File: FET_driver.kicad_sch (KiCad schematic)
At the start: 48 parts, among them Q1 TPH3R704PL,L1Q, Q10 TPH3R704PL,L1Q, Q11 TPH3R704PL,L1Q, Q12 TPH3R704PL,L1Q, Q2 TPH3R704PL,L1Q, Q3 TPH3R704PL,L1Q, Q4 TPH3R704PL,L1Q, Q5 TPH3R704PL,L1Q, Q6 TPH3R704PL,L1Q, Q7 TPH3R704PL,L1Q, Q8 TPH3R704PL,L1Q, Q9 TPH3R704PL,L1Q, U5 FD6288Q, U7 FD6288Q

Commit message: change LED footprint to 0603 and change D1 to more powerful diode with same footprint
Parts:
- D2, D3, D4, D5, D6, D7: Amps (none) -> 4; Voltage (none) -> 40
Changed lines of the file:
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@@
 			)
 		)
+		(property "Amps" "4"
+			(at 101.6 50.8 0)
+			(effects
+				(font
+					(size 1.27 1.27)
+				)
+				(hide yes)
+			)
+		)
+		(property "Voltage" "40"
+			(at 101.6 50.8 0)
+			(effects
+				(font
+					(size 1.27 1.27)
+				)
+				(hide yes)
+			)
+		)
 		(pin "2"
 		)
@@
 			)
 		)
+		(property "Amps" "4"
+			(at 166.37 50.8 0)
+			(effects
+				(font
+					(size 1.27 1.27)
+				)
+				(hide yes)
+			)
+		)
+		(property "Voltage" "40"
+			(at 166.37 50.8 0)
+			(effects
+				(font
+					(size 1.27 1.27)
+				)
+				(hide yes)
+			)
+		)
 		(pin "2"
 		)
@@
 			)
 		)
+		(property "Amps" "4"
+			(at 101.6 124.46 0)
+			(effects
+				(font
+					(size 1.27 1.27)
+				)
+				(hide yes)
+			)
+		)
+		(property "Voltage" "40"
+			(at 101.6 124.46 0)
+			(effects
+				(font
+					(size 1.27 1.27)
+				)
+				(hide yes)
+			)
+		)
 		(pin "2"
 		)
@@
 			)
 		)
+		(property "Amps" "4"
+			(at 233.68 124.46 0)
+			(effects
+				(font
+					(size 1.27 1.27)
+				)
+				(hide yes)
+			)
+		)
+		(property "Voltage" "40"
+			(at 233.68 124.46 0)
+			(effects
+				(font
+					(size 1.27 1.27)
+				)
+				(hide yes)
+			)
+		)
 		(pin "2"
 		)
@@
 			)
 		)
+		(property "Amps" "4"
+			(at 233.68 50.8 0)
+			(effects
+				(font
+					(size 1.27 1.27)
+				)
+				(hide yes)
+			)
+		)
+		(property "Voltage" "40"
+			(at 233.68 50.8 0)
+			(effects
+				(font
+					(size 1.27 1.27)
+				)
+				(hide yes)
+			)
+		)
 		(pin "2"
 		)
@@
 			(at 166.37 124.46 0)
 			(effects
+				(font
+					(size 1.27 1.27)
+				)
+				(hide yes)
+			)
+		)
+		(property "Amps" "4"
+			(at 166.37 124.46 0)
+			(effects
+				(font
+					(size 1.27 1.27)
+				)
+				(hide yes)
+			)
+		)
+		(property "Voltage" "40"
+			(at 166.37 124.46 0)
+			(effects

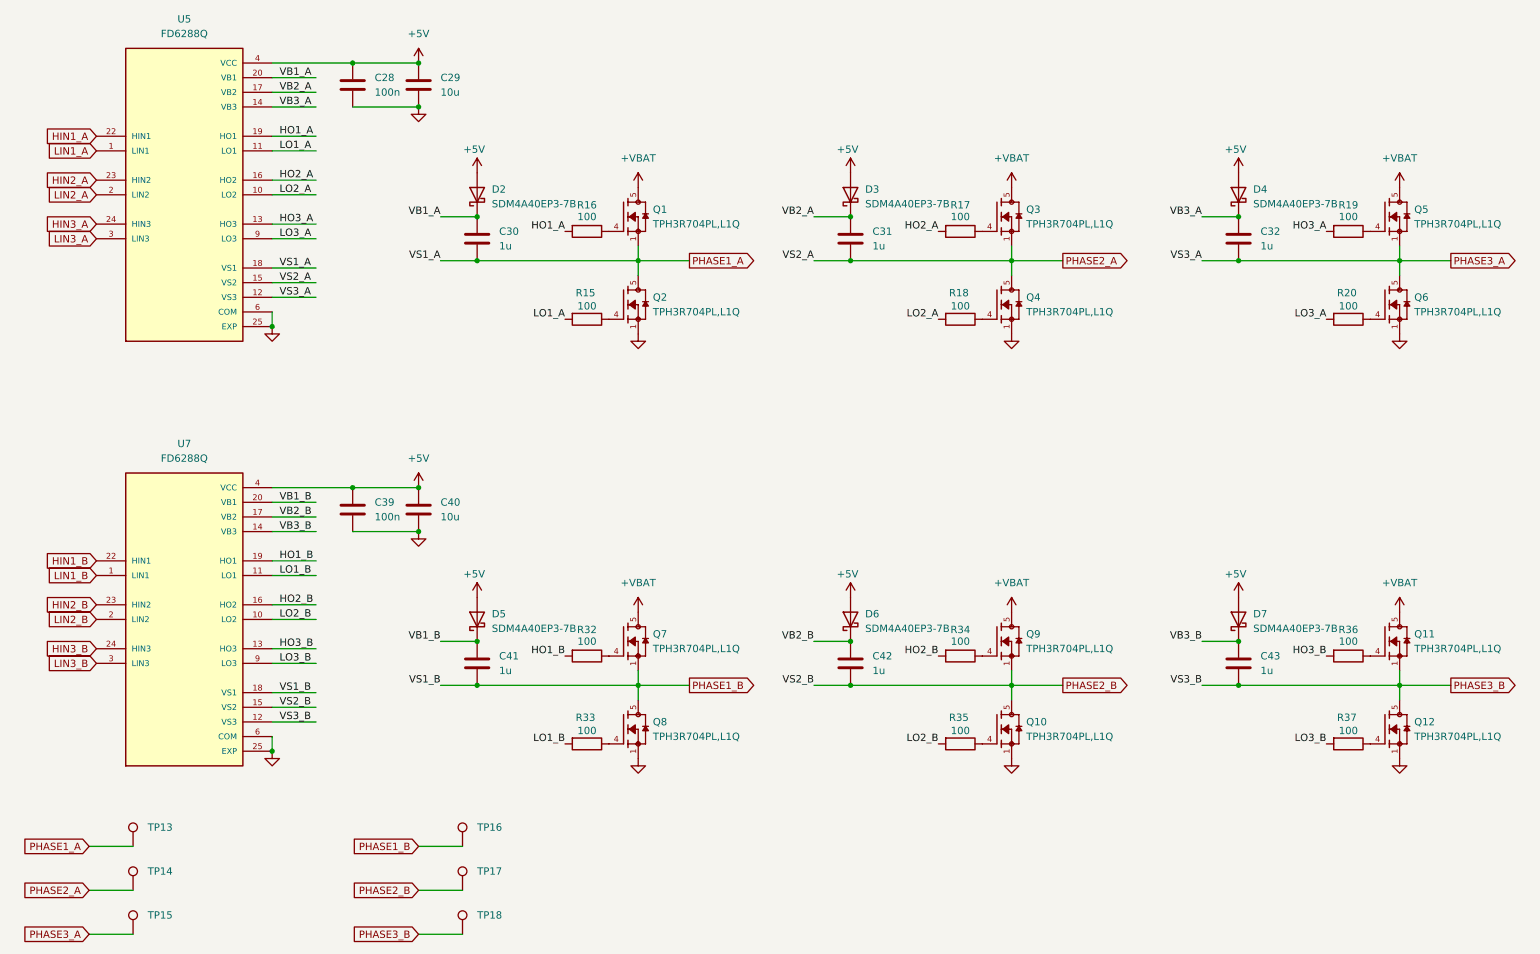
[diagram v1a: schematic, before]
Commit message: edit layout A to work without blind vias by turing MC and ESC 45 to take advantage of pin layouts
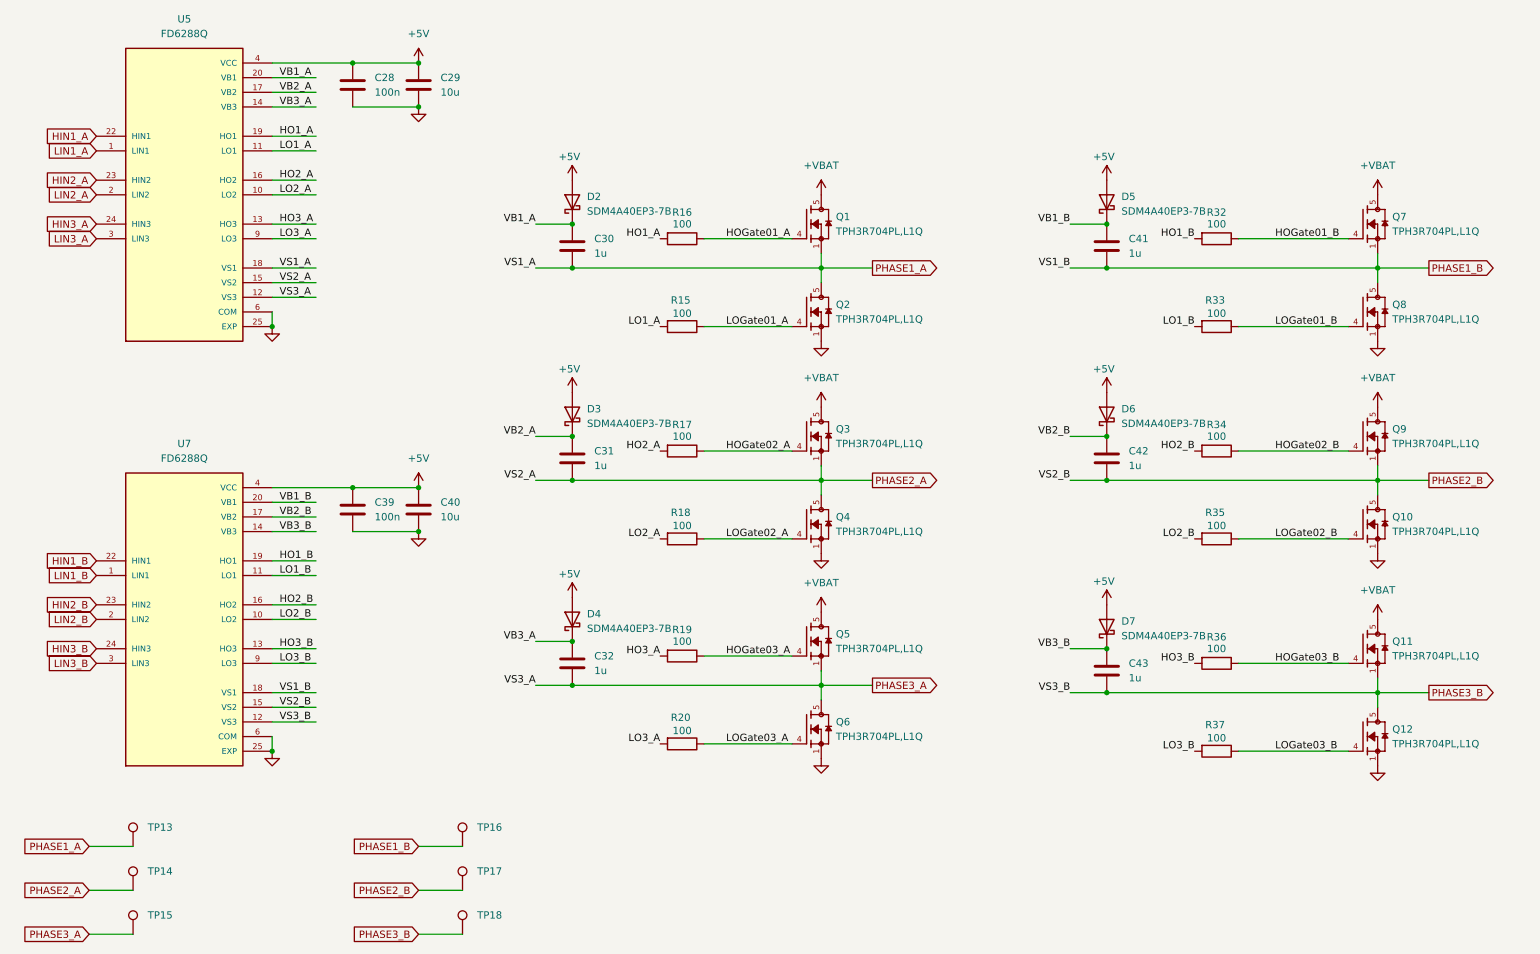
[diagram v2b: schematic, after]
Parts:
- R15, R18, R20: footprint Resistor_SMD:R_0603_1608Metric -> ProjectLibrary:R_0201_0603Metric
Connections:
- net HOGate02_B: now reaches Q9.4, R34.1
- net LOGate02_B: now reaches Q10.4, R35.1
- net HOGate03_B: now reaches Q11.4, R36.1
- net HOGate02_A: now reaches Q3.4, R17.1
- net HOGate03_A: now reaches Q5.4, R19.1
- net LOGate03_A: now reaches Q6.4, R20.1
- net LOGate02_A: now reaches Q4.4, R18.1
- net LOGate01_A: now reaches Q2.4, R15.1
- net HOGate01_B: now reaches Q7.4, R32.1
- net LOGate01_B: now reaches Q8.4, R33.1
- net HOGate01_A: now reaches Q1.4, R16.1
- net LOGate03_B: now reaches Q12.4, R37.1
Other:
- moved on the sheet: C30, C31, C32, C41, C42, C43, D2, D3, D4, D5, D6, D7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

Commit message: removed all microvias, use 0603 for driver resistors
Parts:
- R15, R18, R20: footprint ProjectLibrary:R_0201_0603Metric -> Resistor_SMD:R_0603_1608Metric
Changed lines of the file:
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@@
 			)
 		)
-		(property "Footprint" "ProjectLibrary:R_0201_0603Metric"
+		(property "Footprint" "Resistor_SMD:R_0603_1608Metric"
 			(at 137.16 144.272 90)
 			(effects
@@
 			)
 		)
-		(property "Footprint" "ProjectLibrary:R_0201_0603Metric"
+		(property "Footprint" "Resistor_SMD:R_0603_1608Metric"
 			(at 137.16 108.712 90)
 			(effects
@@
 			)
 		)
-		(property "Footprint" "ProjectLibrary:R_0201_0603Metric"
+		(property "Footprint" "Resistor_SMD:R_0603_1608Metric"
 			(at 137.16 71.882 90)
 			(effects

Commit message: cleanup layout, silkmasks, and add connections between planes for power and gnd
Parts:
- C36: renamed from C28; Tolerance (none) -> 10%
- C37: renamed from C29; Tolerance (none) -> 10%
- C38: renamed from C39; Tolerance (none) -> 10%
- C39: renamed from C40; Tolerance (none) -> 10%
- C40: renamed from C30; Tolerance (none) -> 10%
- C41: renamed from C31; Tolerance (none) -> 10%
- C42: renamed from C32; Tolerance (none) -> 10%
- C43: renamed from C41; Tolerance (none) -> 10%
- C44: renamed from C42; Tolerance (none) -> 10%
- C45: renamed from C43; Tolerance (none) -> 10%
- R31: renamed from R16; value 100 -> 10; Part Number RC0603FR-07100RL -> RC0603FR-0710RL; Tolerance (none) -> 1%
- R32: renamed from R15; value 100 -> 10; Part Number RC0603FR-07100RL -> RC0603FR-0710RL; Tolerance (none) -> 1%
- R33: renamed from R17; value 100 -> 10; Part Number RC0603FR-07100RL -> RC0603FR-0710RL; Tolerance (none) -> 1%
- R34: renamed from R18; value 100 -> 10; Part Number RC0603FR-07100RL -> RC0603FR-0710RL; Tolerance (none) -> 1%
- R35: renamed from R19; value 100 -> 10; Part Number RC0603FR-07100RL -> RC0603FR-0710RL; Tolerance (none) -> 1%
- R36: renamed from R20; value 100 -> 10; Part Number RC0603FR-07100RL -> RC0603FR-0710RL; Tolerance (none) -> 1%
- R37: renamed from R32; value 100 -> 10; Part Number RC0603FR-07100RL -> RC0603FR-0710RL; Tolerance (none) -> 1%
- R38: renamed from R33; value 100 -> 10; Part Number RC0603FR-07100RL -> RC0603FR-0710RL; Tolerance (none) -> 1%
- R39: renamed from R34; value 100 -> 10; Part Number RC0603FR-07100RL -> RC0603FR-0710RL; Tolerance (none) -> 1%
- R40: renamed from R35; value 100 -> 10; Part Number RC0603FR-07100RL -> RC0603FR-0710RL; Tolerance (none) -> 1%
- R41: renamed from R36; value 100 -> 10; Part Number RC0603FR-07100RL -> RC0603FR-0710RL; Tolerance (none) -> 1%
- R42: renamed from R37; value 100 -> 10; Part Number RC0603FR-07100RL -> RC0603FR-0710RL; Tolerance (none) -> 1%
- renumbered D5 to D10, D6 to D11, D7 to D12, D2 to D7, D3 to D8, D4 to D9, U5 to U7, U7 to U8
